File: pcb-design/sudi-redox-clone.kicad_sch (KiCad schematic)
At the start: 109 parts, among them J1 SIDE_CON, J2 0.91 OLED, J4 USBC_PWR_ONLY, J5 SIDE_CON, J7 ARMJTAG, J8 BatCon, K1 KEYSW, K10 KEYSW, K11 KEYSW, K12 KEYSW, K13 KEYSW, K14 KEYSW, K15 KEYSW, K16 KEYSW, K17 KEYSW, K18 KEYSW, K2 KEYSW, K3 KEYSW, K4 KEYSW, K5 KEYSW, K6 KEYSW, K7 KEYSW, K8 KEYSW, K9 KEYSW, U4 AMS1117-3.3, U5 nRF51x22-QFxx, U6 TP4056, U8 MCP23017_SS, Y2 16MHz

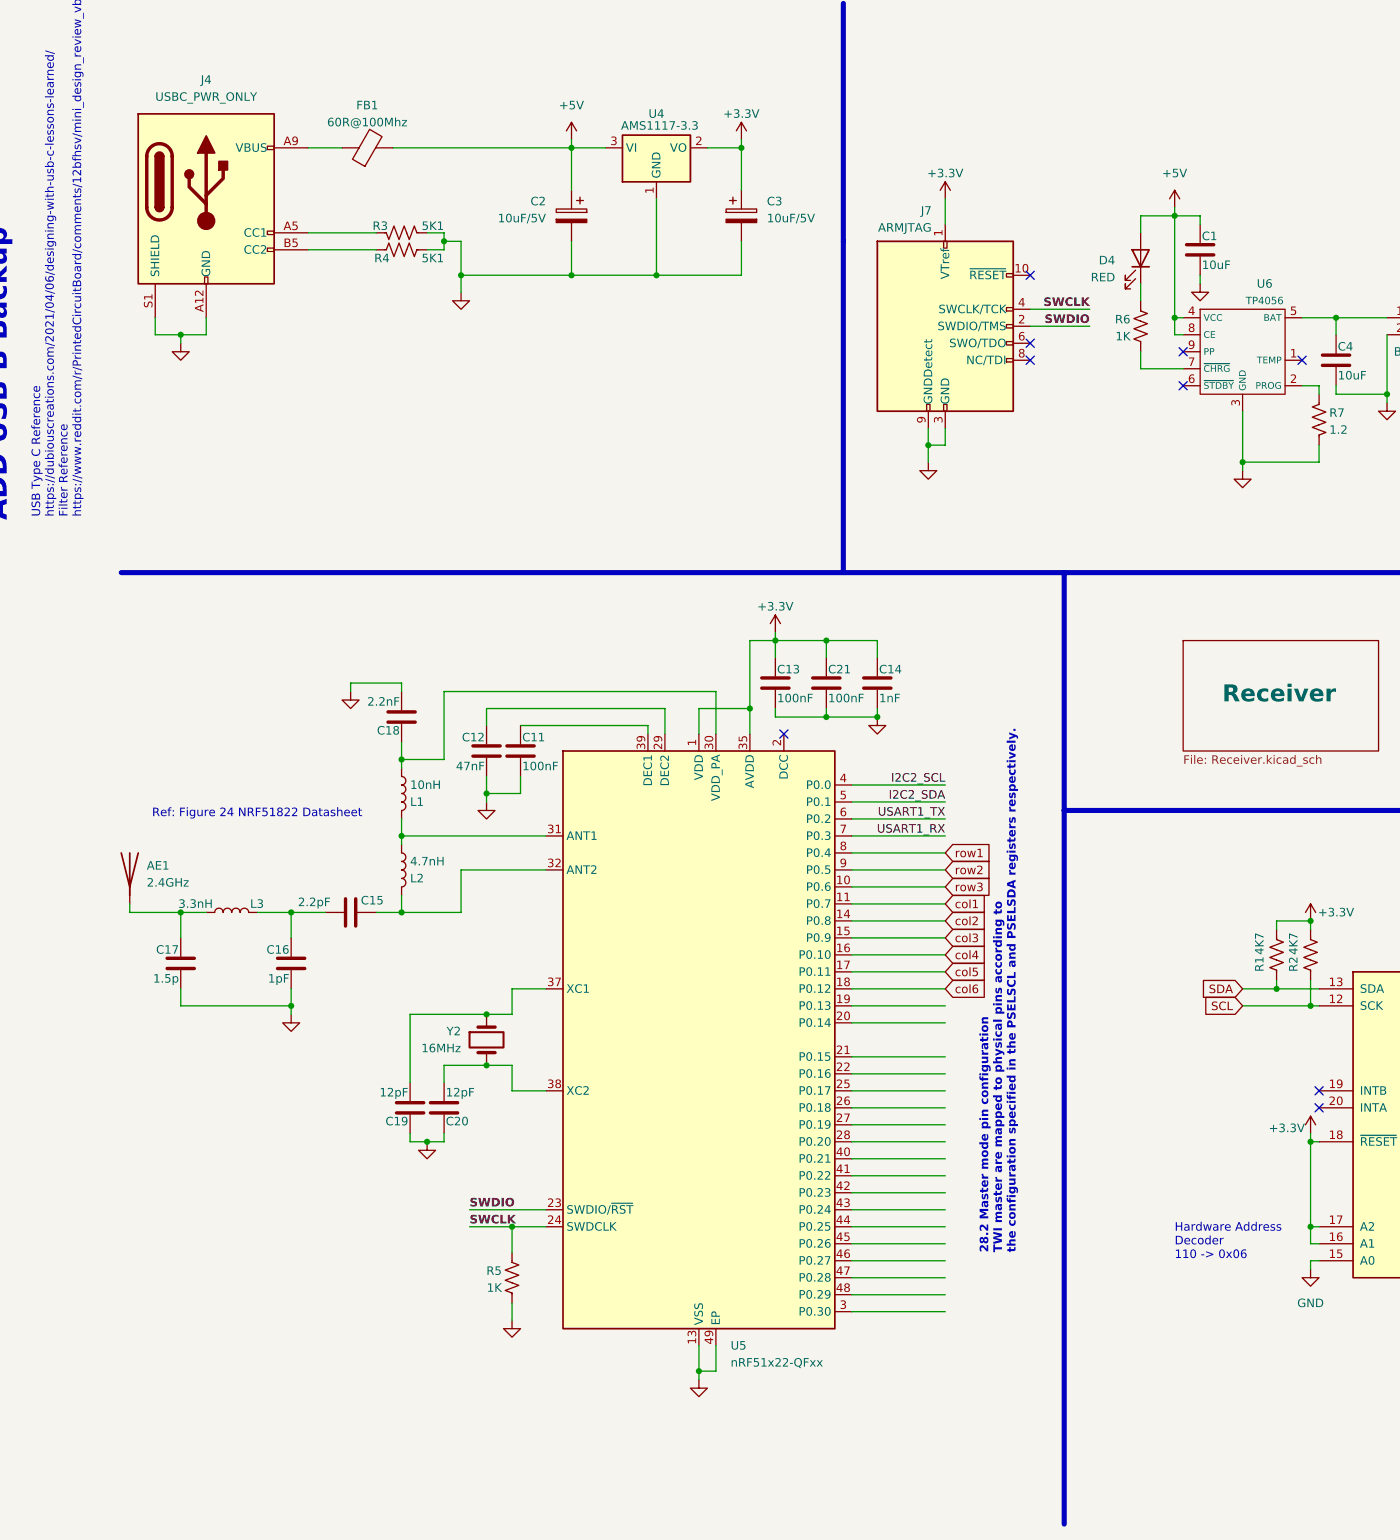
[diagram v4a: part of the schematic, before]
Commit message: change NRF51822 into NRF52832
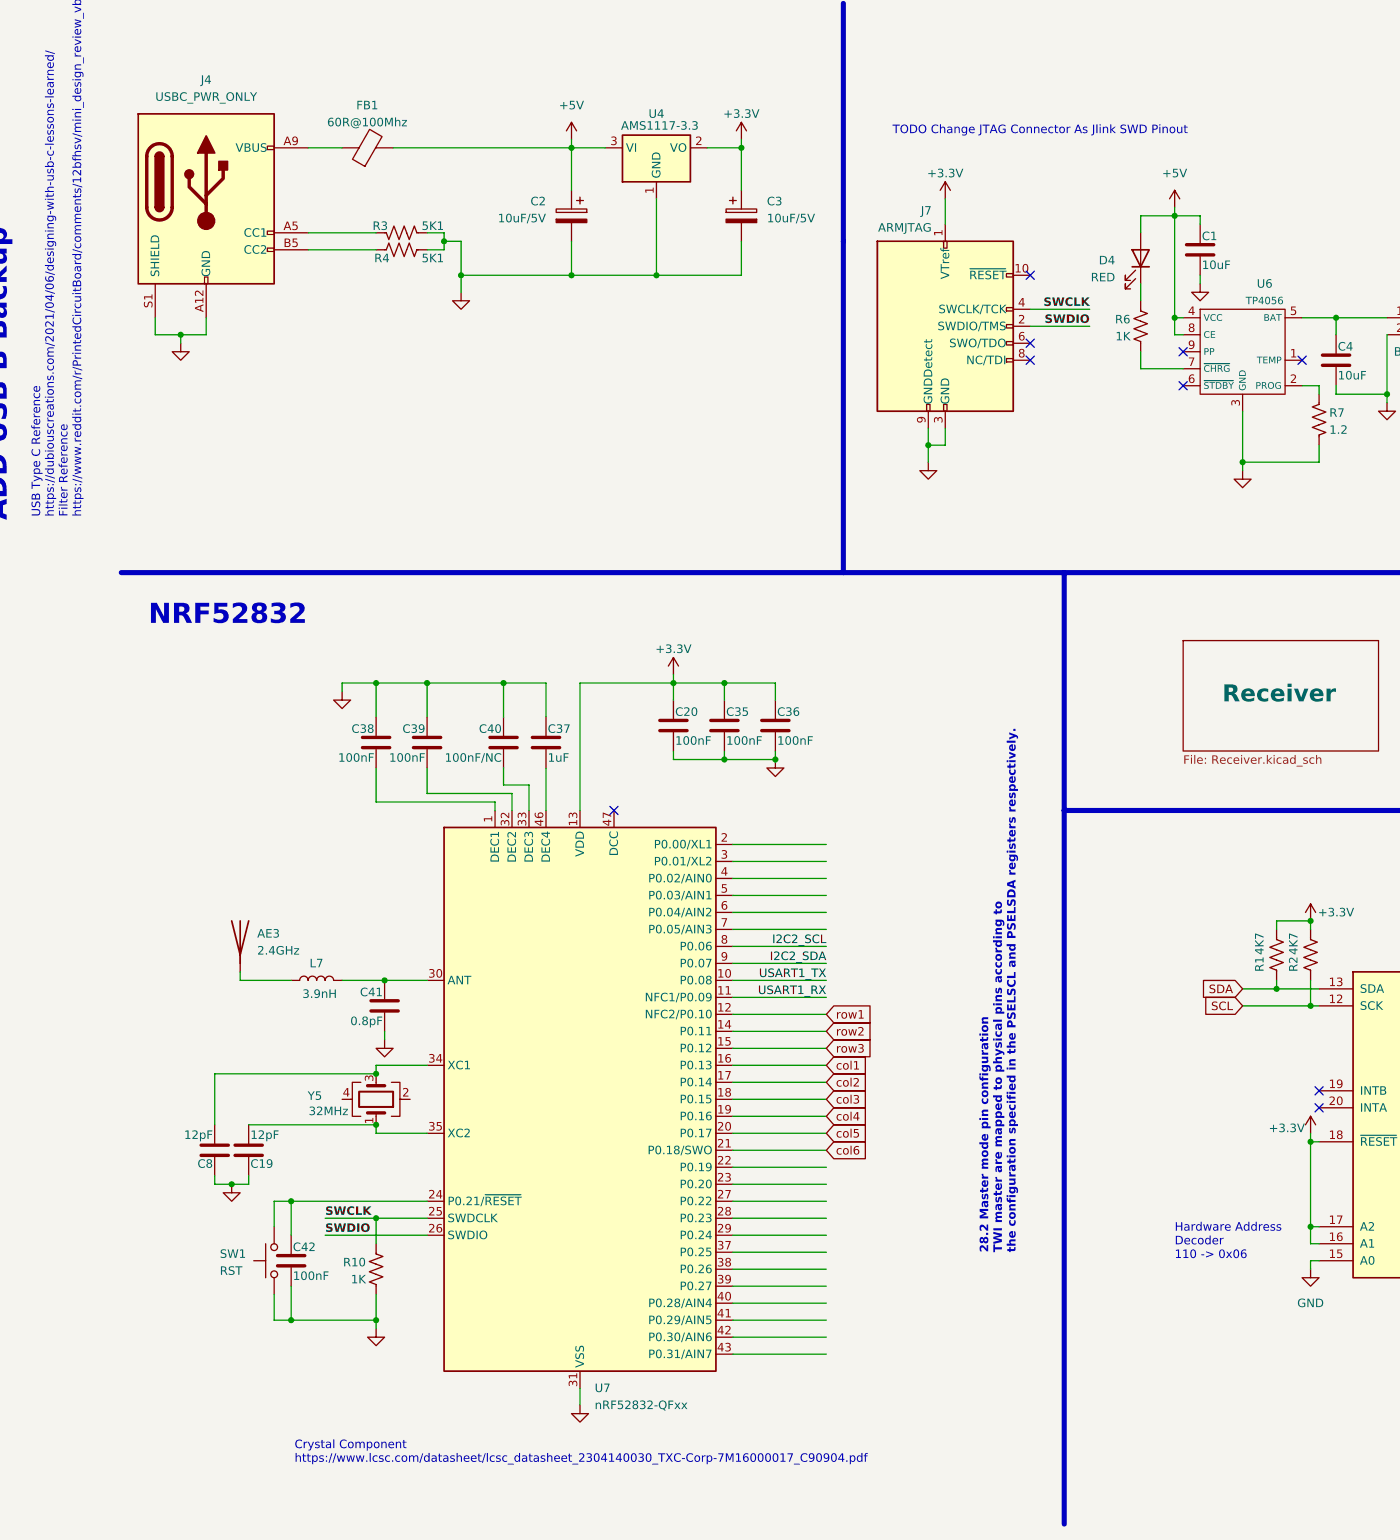
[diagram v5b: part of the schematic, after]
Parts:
- removed AE1: 2.4GHz, RF_Antenna:Texas_SWRA117D_2.4GHz_Left, symbol Device:Antenna
- removed C11, C13, C21: 100nF, Capacitor_SMD:C_0805_2012Metric_Pad1.18x1.45mm_HandSolder, symbol Device:C
- removed C12: 47nF, Capacitor_SMD:C_0805_2012Metric_Pad1.18x1.45mm_HandSolder, symbol Device:C
- removed C14: 1nF, Capacitor_SMD:C_0805_2012Metric_Pad1.18x1.45mm_HandSolder, symbol Device:C
- removed C15: 2.2pF, Capacitor_SMD:C_0805_2012Metric_Pad1.18x1.45mm_HandSolder, symbol Device:C
- removed C16: 1pF, Capacitor_SMD:C_0805_2012Metric_Pad1.18x1.45mm_HandSolder, symbol Device:C
- removed C17: 1.5p, Capacitor_SMD:C_0805_2012Metric_Pad1.18x1.45mm_HandSolder, symbol Device:C
- removed C18: 2.2nF, Capacitor_SMD:C_0805_2012Metric_Pad1.18x1.45mm_HandSolder, symbol Device:C
- removed L1: 10nH, Inductor_SMD:L_0603_1608Metric_Pad1.05x0.95mm_HandSolder, symbol Device:L
- removed L2: 4.7nH, Inductor_SMD:L_0603_1608Metric_Pad1.05x0.95mm_HandSolder, symbol Device:L
- removed L3: 3.3nH, Inductor_SMD:L_0603_1608Metric_Pad1.05x0.95mm_HandSolder, symbol Device:L
- removed R5: 1K, Resistor_SMD:R_0805_2012Metric_Pad1.20x1.40mm_HandSolder, symbol Device:R_US
- removed U5: nRF51x22-QFxx, Package_DFN_QFN:QFN-48-1EP_6x6mm_P0.4mm_EP4.6x4.6mm, symbol MCU_Nordic:nRF51x22-QFxx
- removed Y2: 16MHz, Crystal:Crystal_HC50_Vertical, symbol Device:Crystal
- added AE3: 2.4GHz, RF_Antenna:Texas_SWRA117D_2.4GHz_Left, symbol Device:Antenna
- added C35, C36, C38, C39, C42: 100nF, Capacitor_SMD:C_0805_2012Metric_Pad1.18x1.45mm_HandSolder, symbol Device:C
- added C37: 1uF, Capacitor_SMD:C_0805_2012Metric_Pad1.18x1.45mm_HandSolder, symbol Device:C
- added C40: 100nF/NC, Capacitor_SMD:C_0805_2012Metric_Pad1.18x1.45mm_HandSolder, symbol Device:C
- added C41: 0.8pF, Capacitor_SMD:C_0805_2012Metric_Pad1.18x1.45mm_HandSolder, symbol Device:C
- added C8: 12pF, Capacitor_SMD:C_0805_2012Metric_Pad1.18x1.45mm_HandSolder, symbol Device:C
- added L7: 3.9nH, Inductor_SMD:L_0603_1608Metric_Pad1.05x0.95mm_HandSolder, symbol Device:L
- added R10: 1K, Resistor_SMD:R_0805_2012Metric_Pad1.20x1.40mm_HandSolder, symbol Device:R_US
- added SW1: RST, Button_Switch_SMD:SW_Push_1P1T_NO_6x6mm_H9.5mm, symbol Switch:SW_Push
- added U7: nRF52832-QFxx, Package_DFN_QFN:QFN-48-1EP_6x6mm_P0.4mm_EP4.6x4.6mm, symbol MCU_Nordic:nRF52832-QFxx
- added Y5: 32MHz, Crystal:Crystal_SMD_2016-4Pin_2.0x1.6mm, symbol Device:Crystal_GND24
- C20: value 12pF -> 100nF
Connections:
- net +3.3V: now also C20.1, C35.1, C36.1, U7.13 (VDD), U7.36 (VDD), U7.48 (VDD)
- net GND: now also C20.2, C35.2, C36.2, C37.1, C38.1, C39.1, C40.1, C41.2, C42.2, C8.1, R10.1, SW1.1, U7.31 (VSS), U7.45 (VSS), U7.49 (VSS); no longer C20.1
- net I2C2_SCL: now also U7.8 (P0.06)
- net I2C2_SDA: now also U7.9 (P0.07)
- net SWCLK: now also R10.2, U7.25 (SWDCLK)
- net SWDIO: now also U7.26 (SWDIO)
- net USART1_RX: now also U7.11 (NFC1/P0.09)
- net USART1_TX: now also U7.10 (P0.08)
- net col1: now also U7.16 (P0.13)
- net col2: now also U7.17 (P0.14)
- net col3: now also U7.18 (P0.15)
- net col4: now also U7.19 (P0.16)
- net col5: now also U7.20 (P0.17)
- net col6: now also U7.21 (P0.18/SWO)
- net row1: now also U7.12 (NFC2/P0.10)
- net row2: now also U7.14 (P0.11)
- net row3: now also U7.15 (P0.12)
- net at C19.2: now also U7.35 (XC2), Y5.1
- new net: C8.2, U7.34 (XC1), Y5.3
- new net: C42.1, SW1.2, U7.24 (P0.21/~{RESET})
- new net: C40.2, U7.33 (DEC3)
- new net: AE3.1 (A), L7.1
- new net: C41.1, L7.2, U7.30 (ANT)
- new net: C38.2, U7.1 (DEC1)
- new net: C39.2, U7.32 (DEC2)
- new net: C37.2, U7.46 (DEC4)
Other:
- note added: "Crystal Component https://www.lcsc.com/datasheet/lcsc_datasheet_2304140030_TXC-Corp-7M16000017_C90904.pdf"
- note added: "NRF52832"
- note added: "TODO Change JTAG Connector As Jlink SWD Pinout"
- note removed: "Ref: Figure 24 NRF51822 Datasheet"

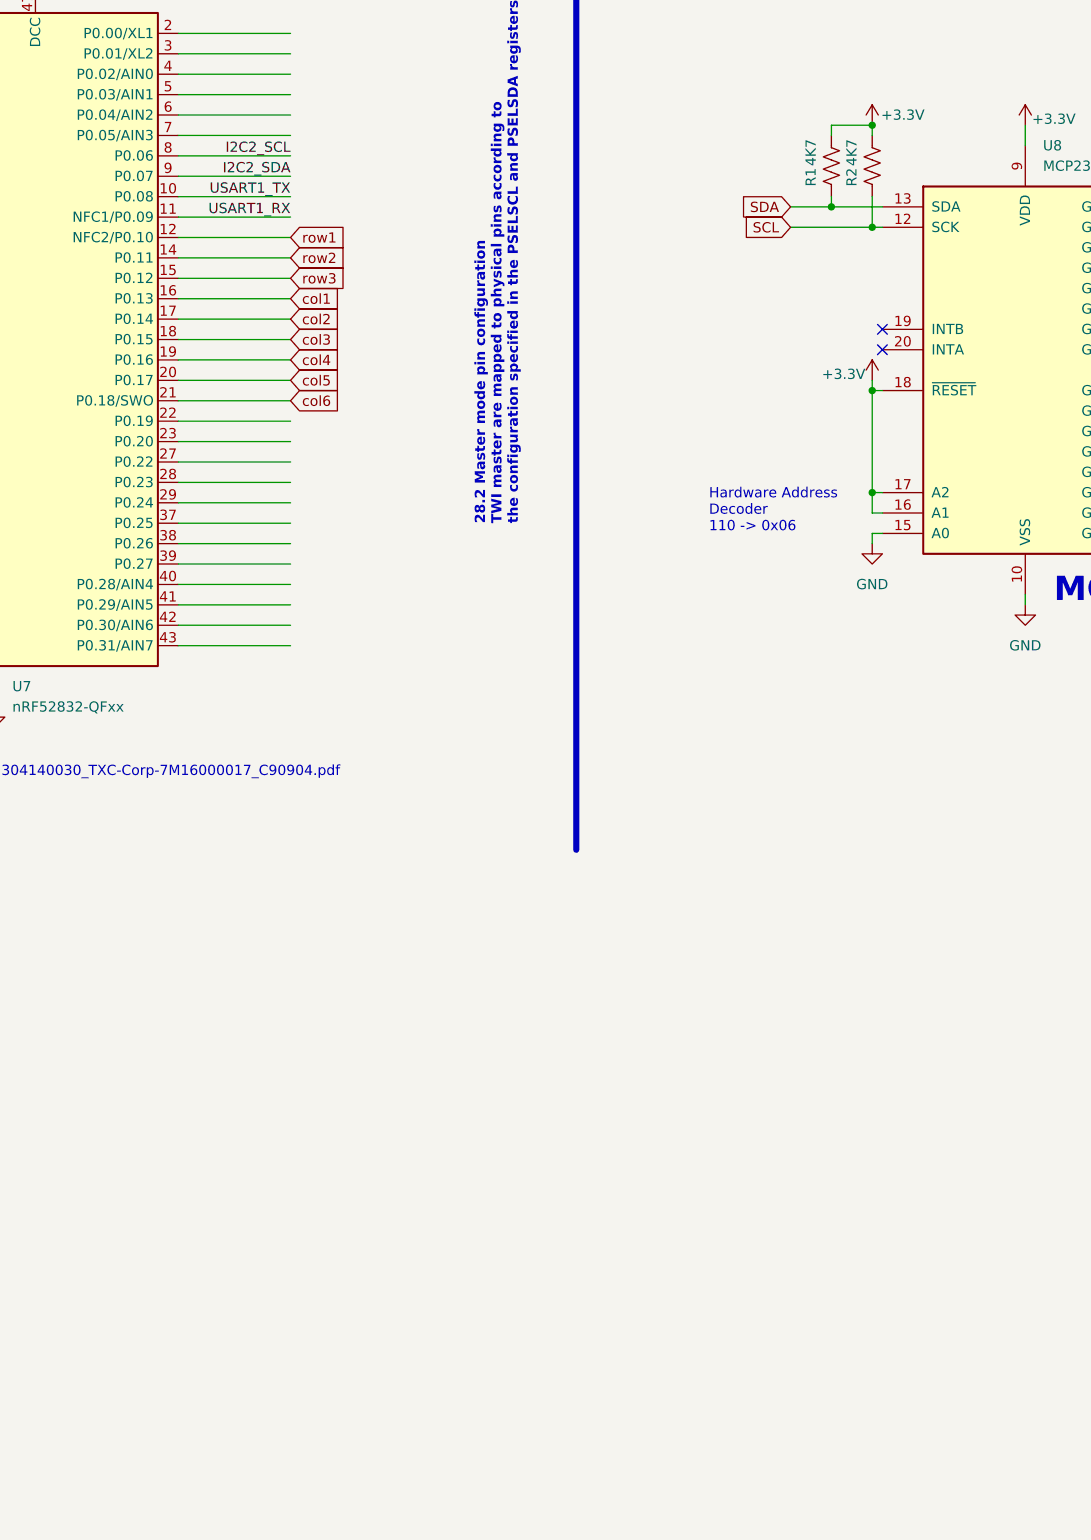
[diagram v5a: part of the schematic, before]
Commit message: updateRoute to use NRF52832
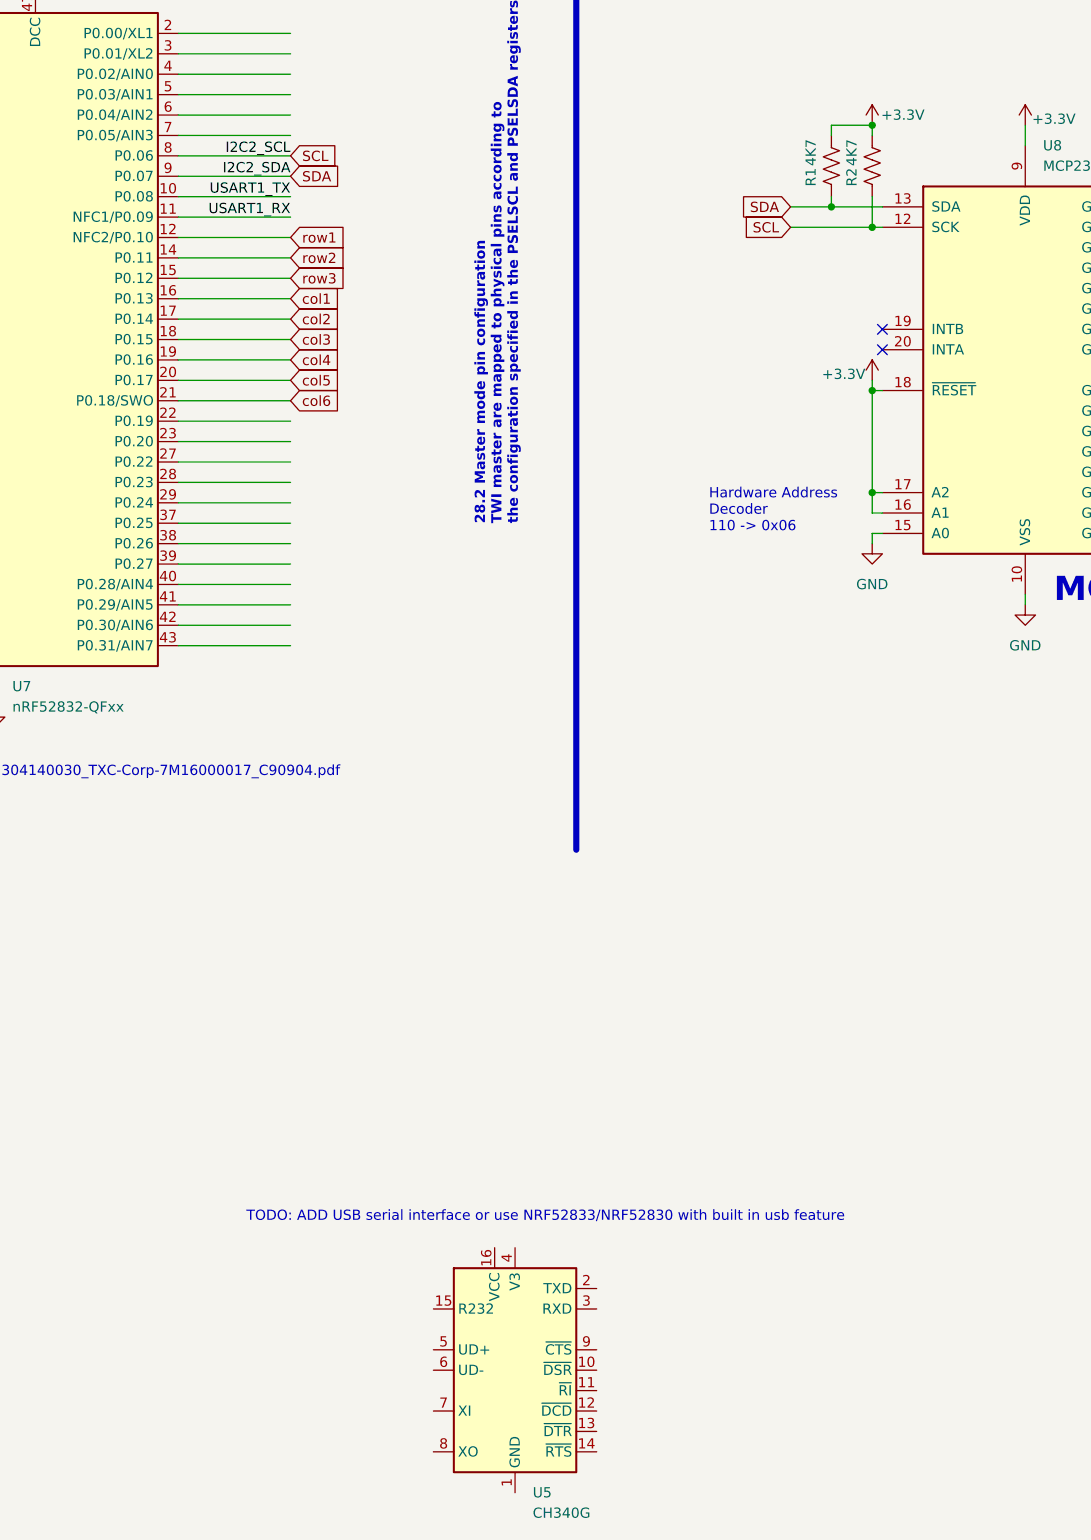
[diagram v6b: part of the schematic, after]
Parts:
- added U5: CH340G, Package_SO:SOIC-16_3.9x9.9mm_P1.27mm, symbol Interface_USB:CH340G
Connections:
- net I2C2_SCL is gone; now on net SCL: U7.8 (P0.06)
- net I2C2_SDA is gone; now on net SDA: U7.9 (P0.07)
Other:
- note added: "TODO: ADD USB serial interface or use NRF52833/NRF52830 with built in usb feature"
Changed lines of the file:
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@@
 		)
 	)
+	(text "TODO: ADD USB serial interface or use NRF52833/NRF52830 with built in usb feature"
+		(exclude_from_sim no)
+		(at 151.13 287.02 0)
+		(effects
+			(font
+				(size 1.27 1.27)
+			)
+		)
+	)
 	(text "Key Matrix"
 		(exclude_from_sim no)
@@
 	(global_label "SDA"
 		(shape input)
+		(at 119.38 157.48 0)
+		(fields_autoplaced yes)
+		(effects
+			(font
+				(size 1.27 1.27)
+			)
+			(justify left)
+		)
+		(property "Intersheetrefs" "${INTERSHEET_REFS}"
+			(at 125.9333 157.48 0)
+			(effects
+				(font
+					(size 1.27 1.27)
+				)
+				(justify left)
+				(hide yes)
+			)
+		)
+	)
+	(global_label "SDA"
+		(shape input)
 		(at 181.61 161.29 180)
 		(fields_autoplaced yes)
@@
 	(global_label "SCL"
 		(shape input)
+		(at 119.38 154.94 0)
+		(fields_autoplaced yes)
+		(effects
+			(font
+				(size 1.27 1.27)
+			)
+			(justify left)
+		)
+		(property "Intersheetrefs" "${INTERSHEET_REFS}"
+			(at 125.8728 154.94 0)
+			(effects
+				(font
+					(size 1.27 1.27)
+				)
+				(justify left)
+				(hide yes)
+			)
+		)
+	)
+	(global_label "SCL"
+		(shape input)
 		(at 181.61 163.83 180)
 		(fields_autoplaced yes)
@@
 					(unit 1)
 				)
+			)
+		)
+	)
+	(symbol
+		(lib_id "Interface_USB:CH340G")
+		(at 147.32 306.07 0)
+		(unit 1)
+		(exclude_from_sim no)
+		(in_bom yes)
+		(on_board yes)
+		(dnp no)
+		(fields_autoplaced yes)
+		(property "Reference" "U5"
+			(at 149.5141 321.31 0)
+			(effects
+				(font
+					(size 1.27 1.27)
+				)
+				(justify left)
+			)
+		)
+		(property "Value" "CH340G"
+			(at 149.5141 323.85 0)
+			(effects
+				(font
+					(size 1.27 1.27)
+				)
+				(justify left)
+			)
+		)
+		(property "Footprint" "Package_SO:SOIC-16_3.9x9.9mm_P1.27mm"
+			(at 148.59 320.04 0)
+			(effects
+				(font
+					(size 1.27 1.27)
+				)
+				(justify left)
+				(hide yes)
+			)
+		)
+		(property "Datasheet" "http://www.datasheet5.com/pdf-local-2195953"
+			(at 138.43 285.75 0)
+			(effects
+				(font
+					(size 1.27 1.27)
+				)
+				(hide yes)
+			)
+		)
+		(property "Description" "USB serial converter, UART, SOIC-16"
+			(at 147.32 306.07 0)
+			(effects
+				(font
+					(size 1.27 1.27)
+				)
+				(hide yes)
+			)
+		)
+		(pin "12"
+		)
+		(pin "16"
+		)
+		(pin "2"
+		)
+		(pin "8"
+		)
+		(pin "14"
+		)
+		(pin "5"
+		)
+		(pin "7"
+		)
+		(pin "6"
+		)
+		(pin "1"
+		)
+		(pin "9"
+		)
+		(pin "10"
+		)
+		(pin "13"
+		)
+		(pin "3"
+		)
+		(pin "11"
+		)
+		(pin "15"
+		)
+		(pin "4"
+		)
+		(instances
+			(project "sudi-redox-clone"
+				(path "/5bbd2338-13ff-49b0-9f87-5cbfec528c5b"
+					(reference "U5")
+					(unit 1)
+				)
